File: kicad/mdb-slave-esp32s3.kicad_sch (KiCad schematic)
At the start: 39 parts, among them J1 MDB_Connector, J2 USB_C_Receptacle_USB2.0_16P, J3 Conn_02x11_Odd_Even, SW1 SW_Push, U1 TLP785, U3 ESP32-S3FH4R2, U4 TLP785, U5 LM2594HVM-3.3, Y1 Crystal_GND24

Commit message: Changing optoacoplator to SOP-4-2.54mm
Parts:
- U1, U4: footprint Package_DIP:SMDIP-4_W7.62mm -> Package_SO:SOP-4_3.8x4.1mm_P2.54mm; LCSC# C41383960 -> C128776
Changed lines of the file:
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@@
 			)
 		)
-		(property "Footprint" "Package_DIP:SMDIP-4_W7.62mm"
+		(property "Footprint" "Package_SO:SOP-4_3.8x4.1mm_P2.54mm"
 			(at 360.68 113.03 0)
 			(effects
@@
 			)
 		)
-		(property "LCSC#" "C41383960"
+		(property "LCSC#" "C128776"
 			(at 365.76 107.95 0)
 			(effects
@@
 			)
 		)
-		(property "Footprint" "Package_DIP:SMDIP-4_W7.62mm"
+		(property "Footprint" "Package_SO:SOP-4_3.8x4.1mm_P2.54mm"
 			(at 370.84 118.11 0)
 			(effects
@@
 			)
 		)
-		(property "LCSC#" "C41383960"
+		(property "LCSC#" "C128776"
 			(at 365.76 123.19 0)
 			(effects

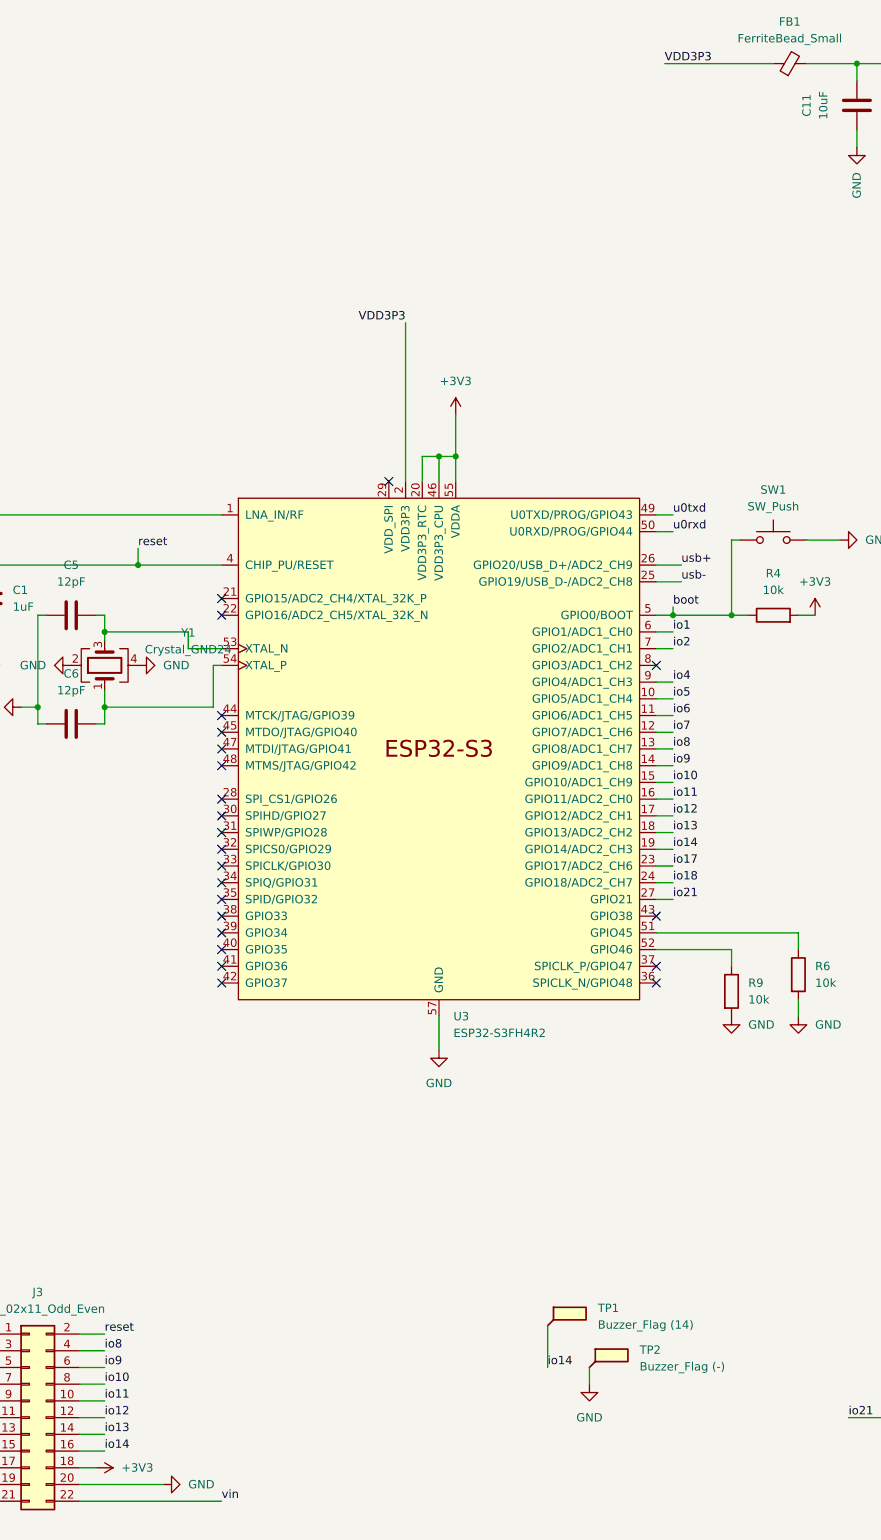
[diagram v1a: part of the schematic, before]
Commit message: Updating optoacoplator package SOP-4_2.54
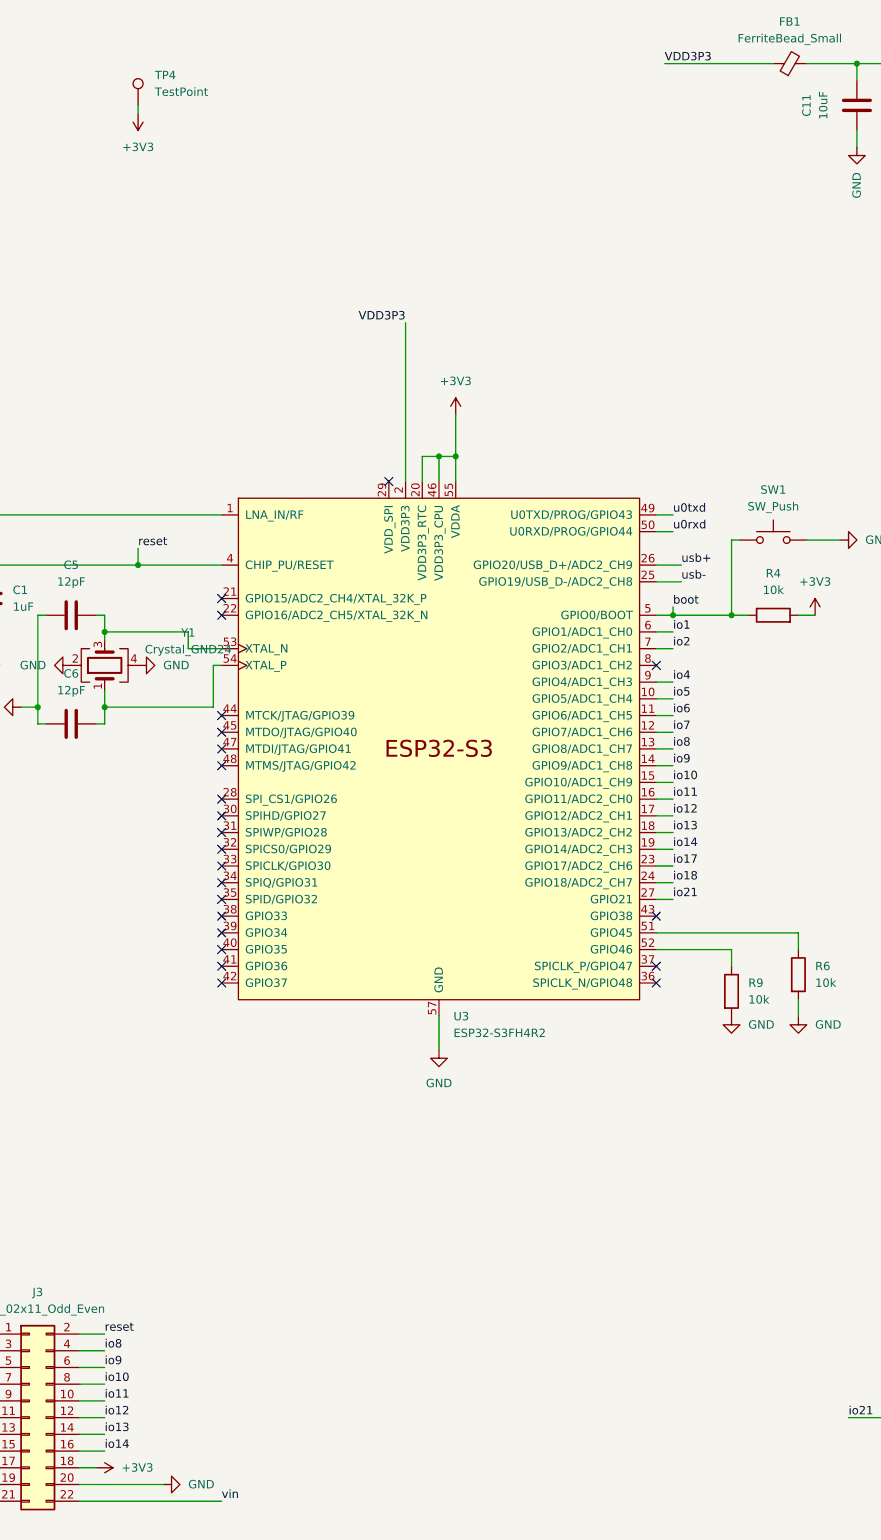
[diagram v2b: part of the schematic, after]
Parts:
- removed TP1: Buzzer_Flag (14), TestPoint:TestPoint_Pad_2.0x2.0mm, symbol Connector:TestPoint_Flag
- removed TP2: Buzzer_Flag (-), TestPoint:TestPoint_Pad_2.0x2.0mm, symbol Connector:TestPoint_Flag
- added TP4: TestPoint, TestPoint:TestPoint_Pad_D1.0mm, symbol Connector:TestPoint
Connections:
- net +3V3: now also TP4.1
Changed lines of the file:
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@@
 	(wire
 		(pts
-			(xy 140.97 222.25) (xy 140.97 228.6)
-		)
-		(stroke
-			(width 0)
-			(type default)
-		)
-	)
-	(wire
-		(pts
 			(xy 356.87 172.72) (xy 351.79 172.72)
 		)
@@
 	(wire
 		(pts
-			(xy 147.32 228.6) (xy 147.32 231.14)
-		)
-		(stroke
-			(width 0)
-			(type default)
-		)
-	)
-	(wire
-		(pts
 			(xy 346.71 125.73) (xy 358.14 125.73)
 		)
@@
 	(wire
 		(pts
+			(xy 78.74 38.1) (xy 78.74 36.83)
+		)
+		(stroke
+			(width 0)
+			(type default)
+		)
+	)
+	(wire
+		(pts
 			(xy 78.74 104.14) (xy 78.74 106.68)
 		)
@@
 		)
 	)
-	(label "io14"
-		(at 140.97 228.6 0)
-		(effects
-			(font
-				(size 1.27 1.27)
-			)
-			(justify left bottom)
-		)
-	)
 	(label "io8"
 		(at 73.66 226.06 0)
@@
 	)
 	(symbol
+		(lib_id "Connector:TestPoint")
+		(at 78.74 36.83 0)
+		(unit 1)
+		(exclude_from_sim no)
+		(in_bom yes)
+		(on_board yes)
+		(dnp no)
+		(fields_autoplaced yes)
+		(property "Reference" "TP4"
+			(at 81.28 32.2579 0)
+			(effects
+				(font
+					(size 1.27 1.27)
+				)
+				(justify left)
+			)
+		)
+		(property "Value" "TestPoint"
+			(at 81.28 34.7979 0)
+			(effects
+				(font
+					(size 1.27 1.27)
+				)
+				(justify left)
+			)
+		)
+		(property "Footprint" "TestPoint:TestPoint_Pad_D1.0mm"
+			(at 83.82 36.83 0)
+			(effects
+				(font
+					(size 1.27 1.27)
+				)
+				(hide yes)
+			)
+		)
+		(property "Datasheet" "~"
+			(at 83.82 36.83 0)
+			(effects
+				(font
+					(size 1.27 1.27)
+				)
+				(hide yes)
+			)
+		)
+		(property "Description" "test point"
+			(at 78.74 36.83 0)
+			(effects
+				(font
+					(size 1.27 1.27)
+				)
+				(hide yes)
+			)
+		)
+		(pin "1"
+		)
+		(instances
+			(project "mdb-slave-esp32s3"
+				(path "/95980b25-0707-441d-ba83-7f6c6e1d1aaa"
+					(reference "TP4")
+					(unit 1)
+				)
+			)
+		)
+	)
+	(symbol
 		(lib_id "power:GND")
 		(at 260.35 172.72 0)
@@
 	(symbol
 		(lib_id "power:GND")
-		(at 147.32 231.14 0)
-		(unit 1)
-		(exclude_from_sim no)
-		(in_bom yes)
-		(on_board yes)
-		(dnp no)
-		(property "Reference" "#PWR031"
-			(at 147.32 237.49 0)
-			(effects
-				(font
-					(size 1.27 1.27)
-				)
-				(hide yes)
-			)
-		)
-		(property "Value" "GND"
-			(at 147.32 236.22 0)
-			(effects
-				(font
-					(size 1.27 1.27)
-				)
-			)
-		)
-		(property "Footprint" ""
-			(at 147.32 231.14 0)
-			(effects
-				(font
-					(size 1.27 1.27)
-				)
-				(hide yes)
-			)
-		)
-		(property "Datasheet" ""
-			(at 147.32 231.14 0)
-			(effects
-				(font
-					(size 1.27 1.27)
-				)
-				(hide yes)
-			)
-		)
-		(property "Description" ""
-			(at 147.32 231.14 0)
-			(effects
-				(font
-					(size 1.27 1.27)
-				)
-				(hide yes)
-			)
-		)
-		(pin "1"
-		)
-		(instances
-			(project "mdb-slave-esp32s3"
-				(path "/95980b25-0707-441d-ba83-7f6c6e1d1aaa"
-					(reference "#PWR031")
-					(unit 1)
-				)
-			)
-		)
-	)
-	(symbol
-		(lib_id "Connector:TestPoint_Flag")
-		(at 140.97 222.25 0)
-		(unit 1)
-		(exclude_from_sim no)
-		(in_bom yes)
-		(on_board yes)
-		(dnp no)
-		(fields_autoplaced yes)
-		(property "Reference" "TP1"
-			(at 148.59 219.5829 0)
-			(effects
-				(font
-					(size 1.27 1.27)
-				)
-				(justify left)
-			)
-		)
-		(property "Value" "Buzzer_Flag (14)"
-			(at 148.59 222.1229 0)
-			(effects
-				(font
-					(size 1.27 1.27)
-				)
-				(justify left)
-			)
-		)
-		(property "Footprint" "TestPoint:TestPoint_Pad_2.0x2.0mm"
-			(at 146.05 222.25 0)
-			(effects
-				(font
-					(size 1.27 1.27)
-				)
-				(hide yes)
-			)
-		)
-		(property "Datasheet" "~"
-			(at 146.05 222.25 0)
-			(effects
-				(font
-					(size 1.27 1.27)
-				)
-				(hide yes)
-			)
-		)
-		(property "Description" "test point (alternative flag-style design)"
-			(at 140.97 222.25 0)
-			(effects
-				(font
-					(size 1.27 1.27)
-				)
-				(hide yes)
-			)
-		)
-		(pin "1"
-		)
-		(instances
-			(project ""
-				(path "/95980b25-0707-441d-ba83-7f6c6e1d1aaa"
-					(reference "TP1")
-					(unit 1)
-				)
-			)
-		)
-	)
-	(symbol
-		(lib_id "power:GND")
 		(at 240.03 81.28 270)
 		(unit 1)
@@
 	)
 	(symbol
+		(lib_id "power:+3V3")
+		(at 78.74 38.1 180)
+		(unit 1)
+		(exclude_from_sim no)
+		(in_bom yes)
+		(on_board yes)
+		(dnp no)
+		(fields_autoplaced yes)
+		(property "Reference" "#PWR032"
+			(at 78.74 34.29 0)
+			(effects
+				(font
+					(size 1.27 1.27)
+				)
+				(hide yes)
+			)
+		)
+		(property "Value" "+3V3"
+			(at 78.74 43.18 0)
+			(effects
+				(font
+					(size 1.27 1.27)
+				)
+			)
+		)
+		(property "Footprint" ""
+			(at 78.74 38.1 0)
+			(effects
+				(font
+					(size 1.27 1.27)
+				)
+				(hide yes)
+			)
+		)
+		(property "Datasheet" ""
+			(at 78.74 38.1 0)
+			(effects
+				(font
+					(size 1.27 1.27)
+				)
+				(hide yes)
+			)
+		)
+		(property "Description" ""
+			(at 78.74 38.1 0)
+			(effects
+				(font
+					(size 1.27 1.27)
+				)
+				(hide yes)
+			)
+		)
+		(pin "1"
+		)
+		(instances
+			(project "mdb-slave-esp32s3"
+				(path "/95980b25-0707-441d-ba83-7f6c6e1d1aaa"
+					(reference "#PWR032")
+					(unit 1)
+				)
+			)
+		)
+	)
+	(symbol
 		(lib_id "Device:L")
 		(at 344.17 172.72 90)
@@
 					(unit 1)
 				)
-			)
-		)
-	)
-	(symbol
-		(lib_id "Connector:TestPoint_Flag")
-		(at 147.32 228.6 0)
-		(unit 1)
-		(exclude_from_sim no)
-		(in_bom yes)
-		(on_board yes)
-		(dnp no)
-		(fields_autoplaced yes)
-		(property "Reference" "TP2"
-			(at 154.94 225.9329 0)
-			(effects
-				(font
-					(size 1.27 1.27)
-				)
-				(justify left)
-			)
-		)
-		(property "Value" "Buzzer_Flag (-)"
-			(at 154.94 228.4729 0)
-			(effects
-				(font
-					(size 1.27 1.27)
-				)
-				(justify left)
-			)
-		)
-		(property "Footprint" "TestPoint:TestPoint_Pad_2.0x2.0mm"
-			(at 152.4 228.6 0)
-			(effects
-				(font
-					(size 1.27 1.27)
-				)
-				(hide yes)
-			)
-		)
-		(property "Datasheet" "~"
-			(at 152.4 228.6 0)
-			(effects
-				(font
-					(size 1.27 1.27)
-				)
-				(hide yes)
-			)
-		)
-		(property "Description" "test point (alternative flag-style design)"
-			(at 147.32 228.6 0)
-			(effects
-				(font
-					(size 1.27 1.27)
-				)
-				(hide yes)
-			)
-		)
-		(pin "1"
-		)
-		(instances
-			(project "mdb-slave-esp32s3"
-				(path "/95980b25-0707-441d-ba83-7f6c6e1d1aaa"
-					(reference "TP2")
-					(unit 1)
-				)

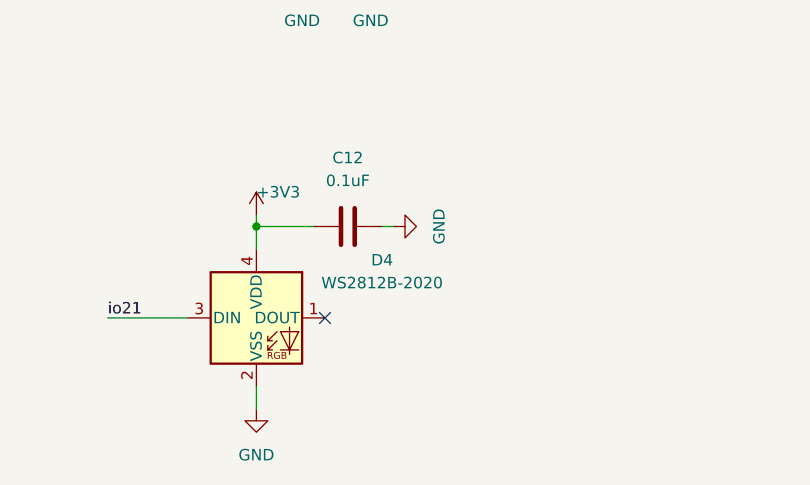
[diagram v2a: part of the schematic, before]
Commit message: Replace ESP32-S3FH4R2 Mouser -> LCSC
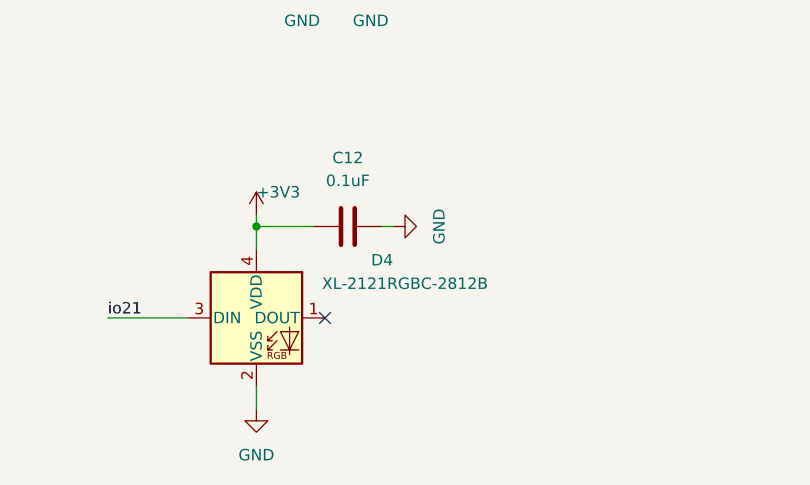
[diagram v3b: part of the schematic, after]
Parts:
- D4: value WS2812B-2020 -> XL-2121RGBC-2812B
- U3: LCSC# (none) -> C3013940; MOUSER# 356-ESP32-S3FH4R2 -> (none)
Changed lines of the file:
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@@
 		(on_board yes)
 		(dnp no)
-		(fields_autoplaced yes)
 		(property "Reference" "D4"
 			(at 217.17 229.7998 0)
@@
 			)
 		)
-		(property "Value" "WS2812B-2020"
-			(at 217.17 232.3398 0)
+		(property "Value" "XL-2121RGBC-2812B"
+			(at 219.71 232.41 0)
 			(effects
 				(font
@@
 			)
 		)
-		(property "MOUSER#" "356-ESP32-S3FH4R2 "
+		(property "LCSC#" "C3013940"
 			(at 124.46 134.62 0)
 			(effects
